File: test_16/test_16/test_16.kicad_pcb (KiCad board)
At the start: 2 copper layers, 100 x 100 mm, 81 parts, among them J1 Array set 0, J2 Array set 0

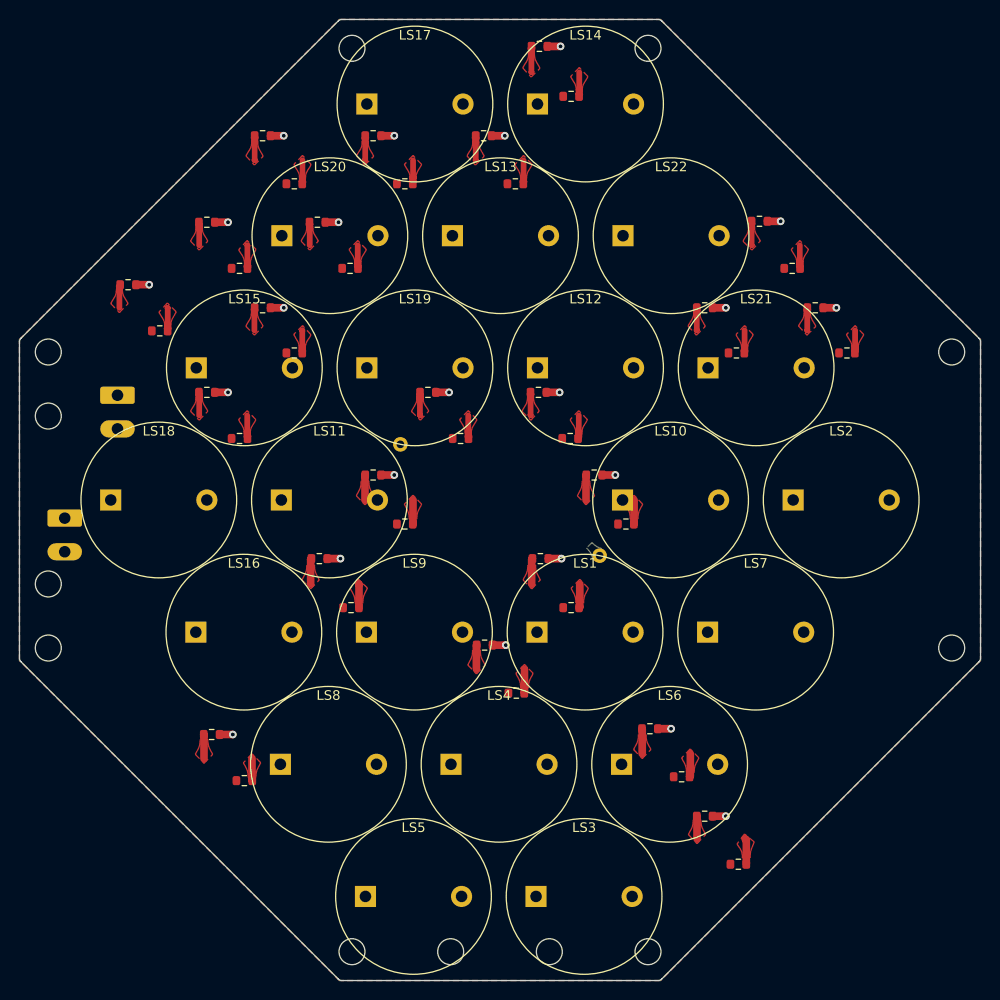
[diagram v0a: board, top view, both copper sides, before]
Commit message: bracket alignement
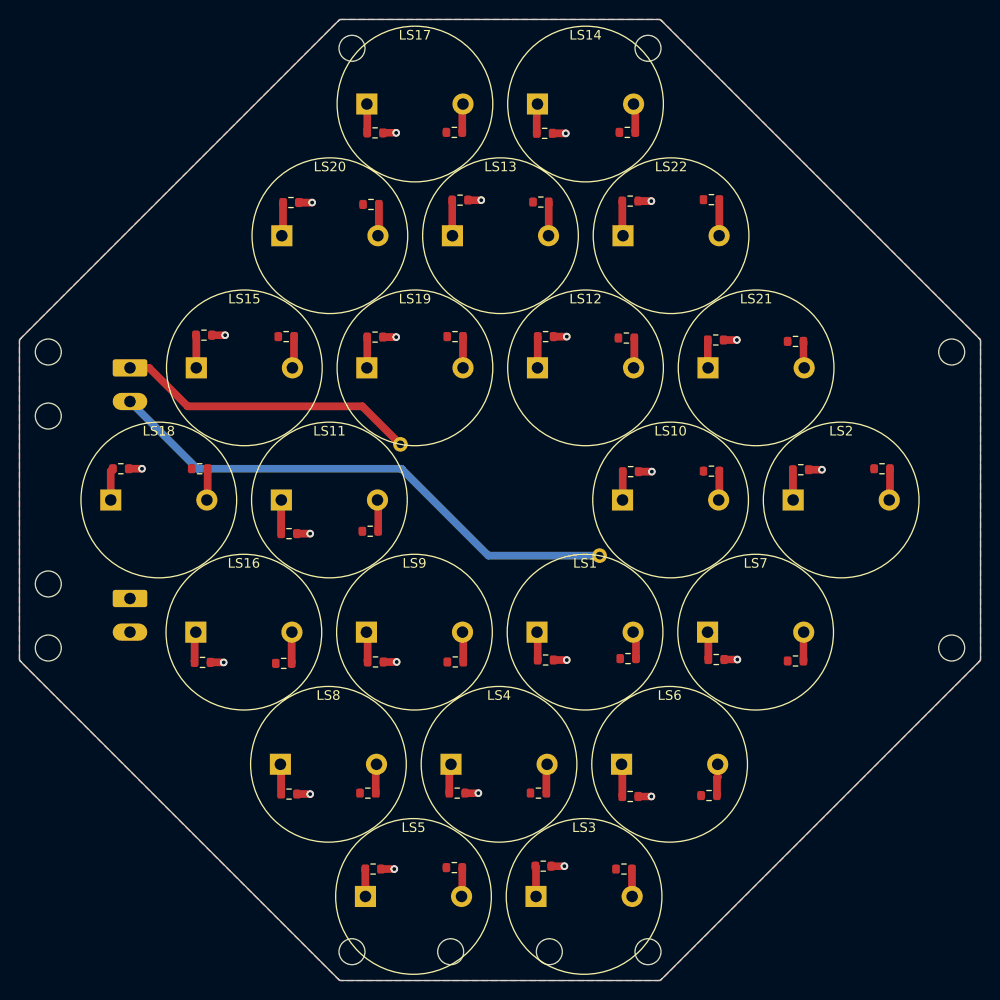
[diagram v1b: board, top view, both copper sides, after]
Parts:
- moved R28 74.2 mm to (360.6, 246.8)
- moved R6 73.8 mm to (413.6, 280.9)
- moved R16 71.1 mm to (421.8, 280.8)
- moved R3 71.0 mm to (404.5, 288.1)
- moved R17 70.8 mm to (430.8, 266.8)
- moved R7 69.9 mm to (422.5, 266.6)
- moved R13 68.7 mm to (412.9, 288.4)
- moved R38 68.4 mm to (368.8, 246.8)
- moved R34 59.5 mm to (413.2, 211.8)
- moved R9 56.0 mm to (387.1, 266.9)
- moved R8 55.6 mm to (378.1, 280.6)
- moved R4 54.4 mm to (395.6, 280.5)
- moved R43 53.9 mm to (430.8, 233.5)
- moved R24 53.6 mm to (404.6, 211.8)
- moved R18 52.7 mm to (386.2, 280.5)
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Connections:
- J2 pad 1: Net-(D1-Pad1) -> Net-(D1-Pad2)
- J2 pad 2: Net-(D1-Pad2) -> Net-(D1-Pad1)
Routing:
- net Net-(D1-Pad1): track 0.00 -> 55.5 mm
- net Net-(D1-Pad2): track 0.00 -> 31.4 mm
- net Net-(LS22-Pad2): track 2.51 -> 3.76 mm
- net Net-(LS11-Pad1): track 2.36 -> 3.51 mm
- net Net-(LS20-Pad1): track 2.41 -> 3.50 mm
- net Net-(LS22-Pad1): track 2.61 -> 3.63 mm
- net Net-(LS13-Pad1): track 2.71 -> 3.71 mm
- net Net-(LS13-Pad2): track 2.51 -> 3.51 mm
- net Net-(LS18-Pad1): track 2.36 -> 3.34 mm
- net Net-(LS18-Pad2): track 2.36 -> 3.28 mm
- net Net-(LS11-Pad2): track 2.36 -> 3.28 mm
- net Net-(LS20-Pad2): track 2.41 -> 3.29 mm
- net Net-(LS15-Pad2): track 2.48 -> 3.32 mm
- net Net-(LS6-Pad2): track 2.46 -> 3.28 mm
- net Net-(LS6-Pad1): track 2.56 -> 3.38 mm
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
